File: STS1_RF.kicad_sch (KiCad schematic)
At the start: 74 parts, among them J1 UHF, Q1 SQ2318, U10 TQP3M9036, U11 QPC1022, U2 LP2985-1.8, U4 74LVC2G74, U5 TYKTBCSANF-26.000000, U7 NL17SV04XV5T2G, U8 Si4463, U9 LFCG-490+

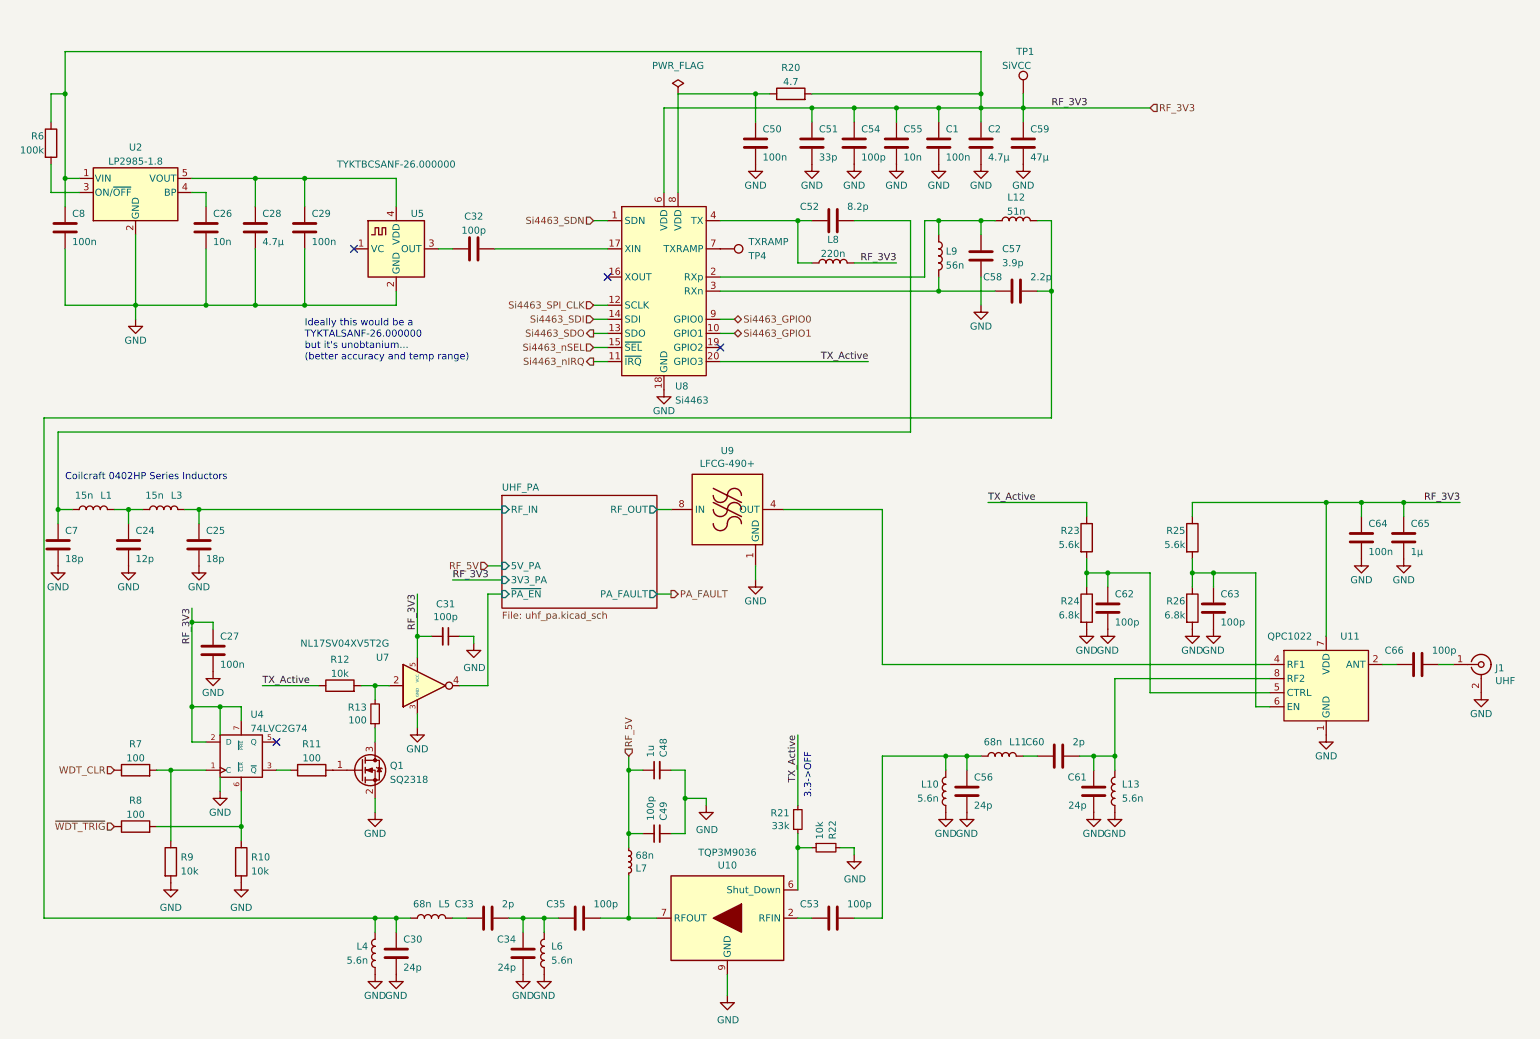
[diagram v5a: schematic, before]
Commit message: feat: clean up schematic
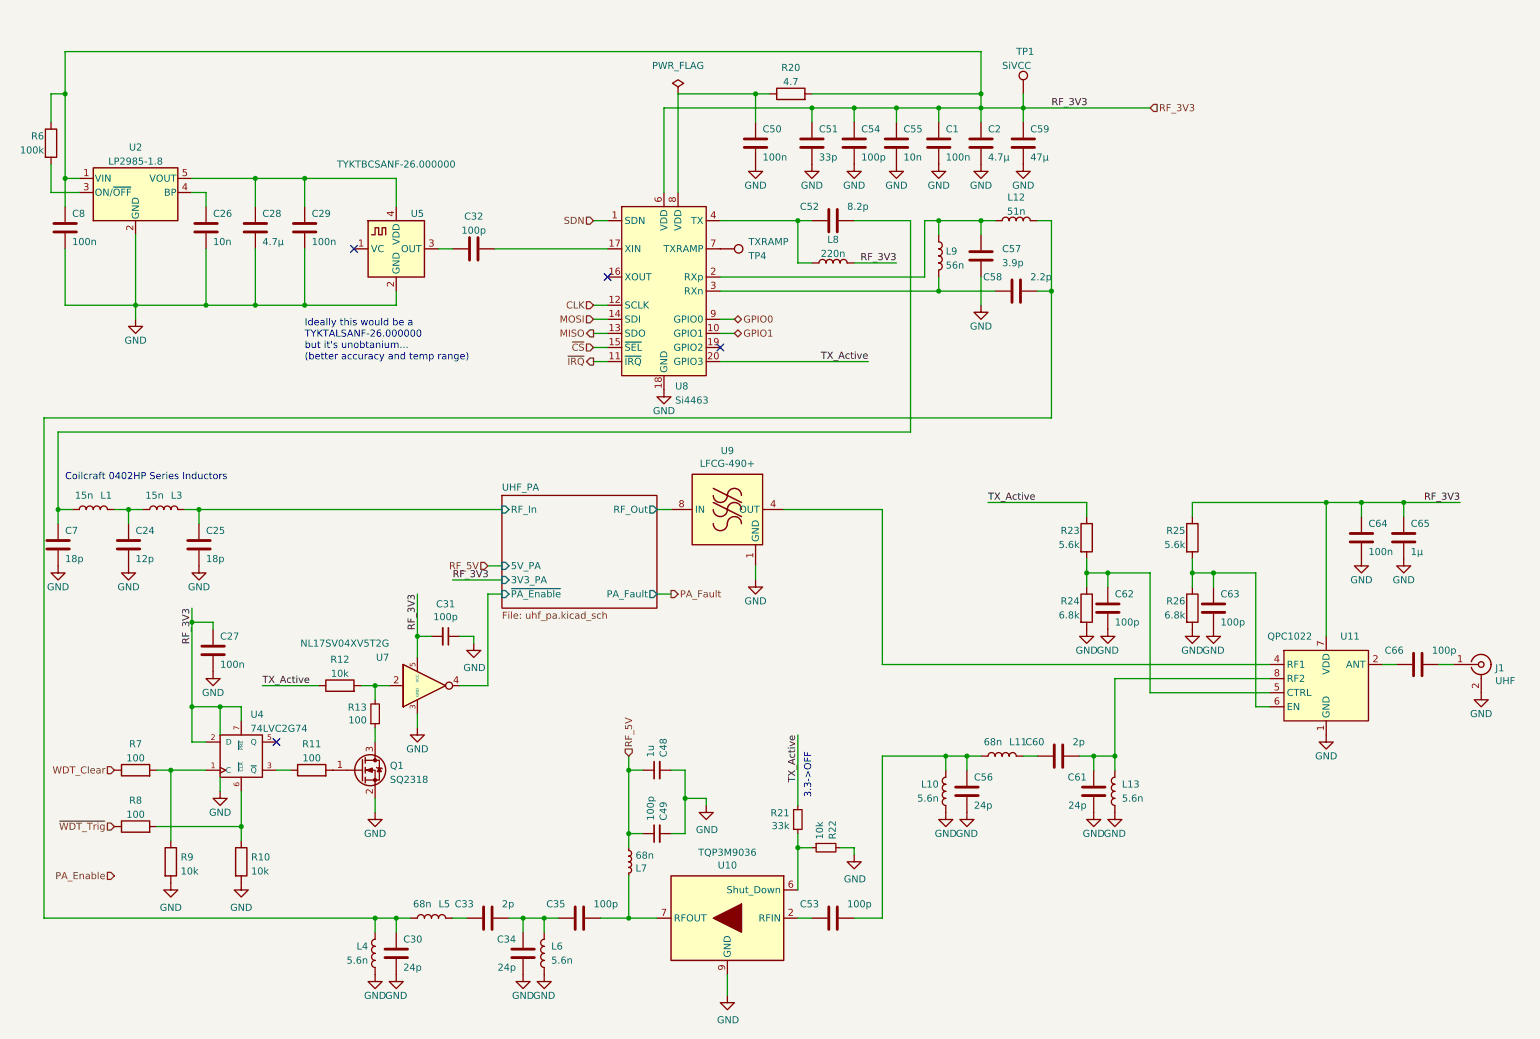
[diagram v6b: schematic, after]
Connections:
- net Si4463_GPIO0 renamed GPIO0
- net Si4463_GPIO1 renamed GPIO1
- net Si4463_SDI renamed MOSI
- net Si4463_SDN renamed SDN
- net Si4463_SDO renamed MISO
- net Si4463_SPI_CLK renamed CLK
- net Si4463_nIRQ renamed ~{IRQ}
- net Si4463_nSEL renamed ~{CS}
- net UHF_PA/RF_IN renamed UHF_PA/RF_In
- net UHF_PA/RF_OUT renamed UHF_PA/RF_Out
- net UHF_PA/~{PA_EN} renamed UHF_PA/~{PA_Enable}
- net WDT_CLR renamed WDT_Clear
- net ~{WDT_TRIG} renamed ~{WDT_Trig}
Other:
- sheet UHF_PA ports: added PA_Fault, RF_In, RF_Out, ~{PA_Enable}; removed PA_FAULT, RF_IN, RF_OUT, ~{PA_EN}

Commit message: feat: update RF hardware and clean up ERC errors
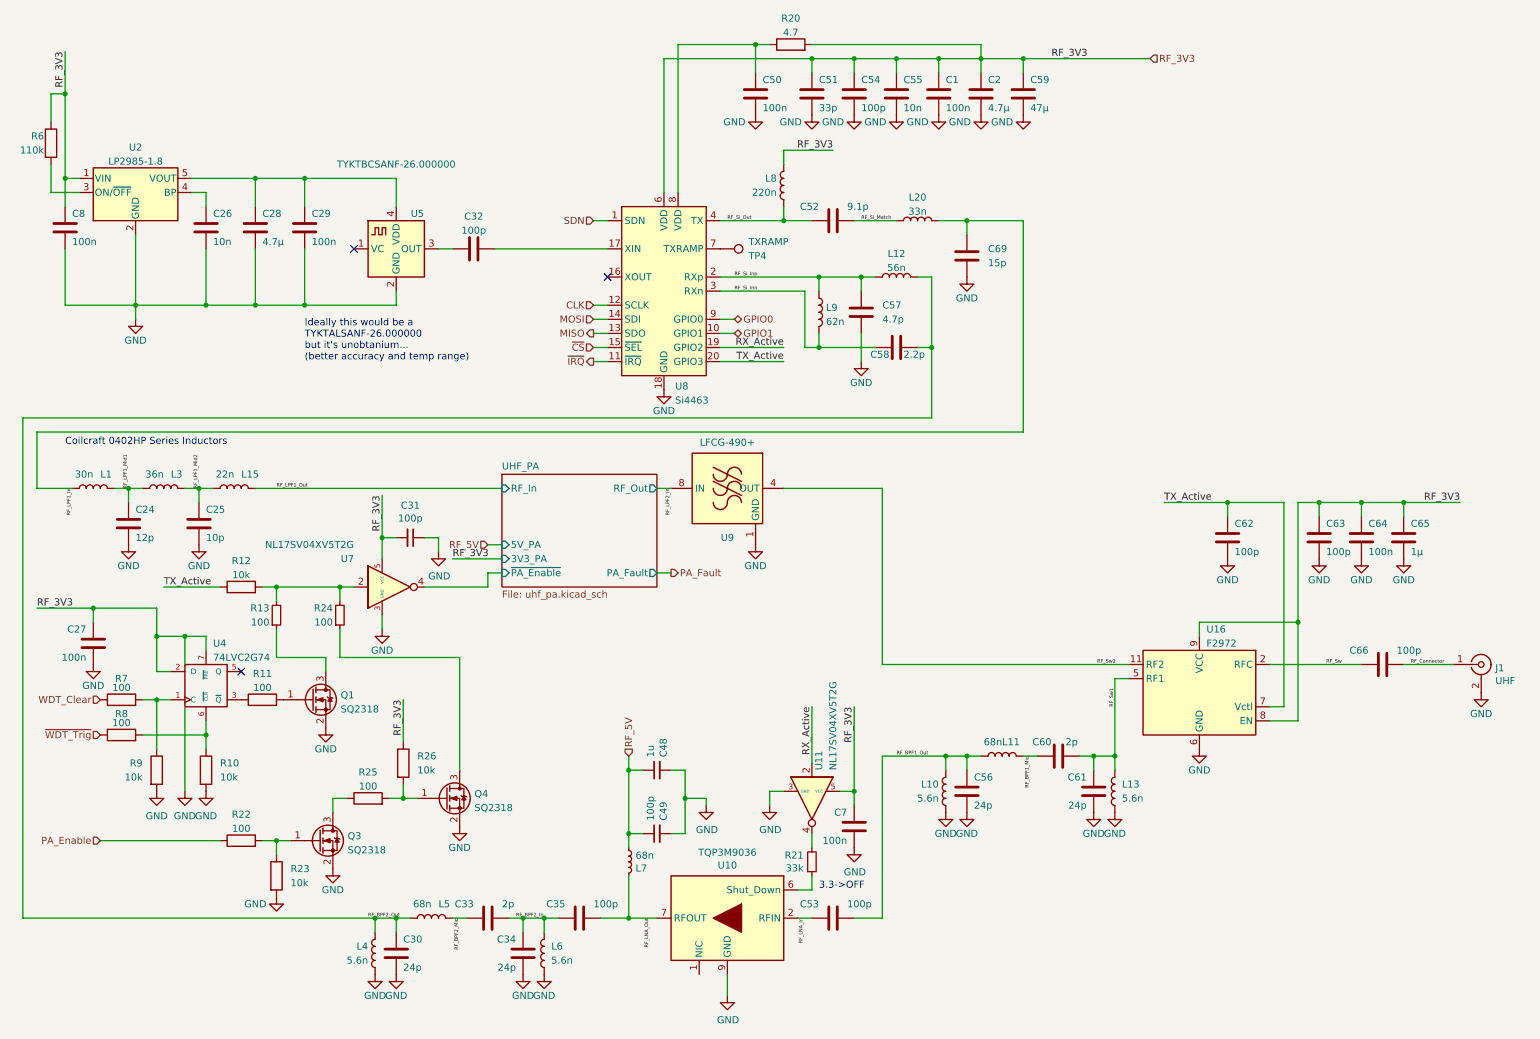
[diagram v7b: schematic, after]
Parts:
- removed R22: 10k, Resistor_SMD:R_0603_1608Metric, symbol Device:R_Small
- removed R24: 6.8k, Resistor_SMD:R_0603_1608Metric, symbol Device:R
- removed TP1: SiVCC, STS1library:STS1_Testpoint, symbol Connector:TestPoint
- removed U11: QPC1022, STS_Package_LGA:Qorvo_9Pin_1.1x1.5mm_LGA, symbol STS_RF_Module:QPC1022
- added C69: 15p, Capacitor_SMD:C_0402_1005Metric, symbol Device:C
- added L15: 22n, Inductor_SMD:L_0402_1005Metric, symbol Device:L
- added L20: 33n, Inductor_SMD:L_0402_1005Metric, symbol Device:L
- added Q3, Q4: SQ2318, Package_TO_SOT_SMD:SOT-23, symbol Device:Q_NMOS_GSD
- added R22: 100, Resistor_SMD:R_0603_1608Metric, symbol Device:R
- added R24: 100, Resistor_SMD:R_0603_1608Metric, symbol Device:R_Small
- added U11: NL17SV04XV5T2G, Package_TO_SOT_SMD:SOT-553, symbol 74xGxx:74LVC1GU04DRL
- added U16: F2972, Package_DFN_QFN:IDT_NEG12_1EP_2x2mm_P0.5mm_EP1.1x1.1mm_ThermalVias, symbol lsf-kicad-lib:F2972
- C25: value 18p -> 10p
- C52: value 8.2p -> 9.1p
- C57: value 3.9p -> 4.7p
- C7: value 18p -> 100n; footprint Capacitor_SMD:C_0402_1005Metric -> Capacitor_SMD:C_0805_2012Metric
- L1: value 15n -> 30n
- L12: value 51n -> 56n
- L3: value 15n -> 36n
- L9: value 56n -> 62n
- R23: value 5.6k -> 10k
- R25: value 5.6k -> 100
- R26: value 6.8k -> 10k
- R6: value 100k -> 110k
- U10: symbol lsf-kicad:TQP3M9036 -> lsf-kicad-lib:TQP3M9036
- U9: symbol lsf-kicad:LFCG-490+ -> lsf-kicad-lib:LFCG-490+
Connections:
- net GND: now also R23.2, C69.2, Q3.2 (S), Q4.2 (S), U11.3 (GND), U16.1 (GND), U16.10 (GND), U16.12 (GND), U16.13 (GND), U16.3 (GND), U16.4 (GND), U16.6 (GND); no longer R26.2
- net PA_Enable: now also R22.1
- net TX_Active: now also C62.1, U16.7 (Vctl); no longer R21.2, R23.1
- net VCC: now also C63.1, C7.1, R26.1, U11.5 (VCC), U16.8 (EN), U16.9 (VCC); no longer R25.1
- net RF_Connector: now reaches C66.2, J1.1 (In)
- net at R12.2, R13.2, U7.2: now also R24.2
- net RF_Sw2: now reaches U9.4 (OUT)
- net RF_Sw2: now also U16.11 (RF2)
- net RF_BPF2_Out: now reaches C30.1, C58.2, L12.2, L4.2, L5.1
- net RF_BPF2_In: now reaches C33.2, C34.1, C35.1, L6.2
- net RF_LNA_Out: now reaches C35.2, L7.1, U10.7 (RFOUT)
- net RF_LPF1_Mid1: now reaches C24.1, L1.2, L3.1
- net RF_BPF2_Mid: now reaches C33.1, L5.2
- net RF_BPF1_Mid: now reaches C60.1, L11.2
- net RF_Sw1: now reaches C60.2, C61.1, L13.2
- net RF_Sw1: now also U16.5 (RF1)
- net RF_Si_Out: now reaches C52.1, L8.1, U8.4 (TX)
- net RF_BPF1_Out: now reaches C53.2, C56.1, L10.2, L11.1
- net RF_LNA_In: now reaches C53.1, U10.2 (RFIN)
- net at U10.1 (NIC): now also U10.3 (NIC), U10.4 (NIC), U10.5 (NIC), U10.8 (NIC)
- net RF_Si_Inp: now reaches C57.1, L12.1, L9.1, U8.2 (RXp)
- net RF_Si_Inn: now reaches C58.1, L9.2, U8.3 (RXn)
- net RF_Sw: now reaches C66.1
- net RF_Sw: now also U16.2 (RFC)
- net RX_Active: now reaches U8.19 (GPIO2)
- net RX_Active: now also U11.2
- net UHF_PA/RF_In renamed RF_LPF1_Mid2
- net RF_LPF1_Mid2: now also L15.1
- net UHF_PA/RF_Out renamed RF_LPF2_In
- new net: R21.2, U11.4
- new net: Q3.1 (G), R22.2, R23.1
- new net: Q3.3 (D), R25.1
- new net: Q4.1 (G), R25.2, R26.2
- new net: Q4.3 (D), R24.1
- new net RF_LPF1_In: C69.1, L1.1, L20.2
- new net RF_LPF1_Out: L15.2
- new net RF_Si_Match: C52.2, L20.1
- no-connect marks 4 -> 3
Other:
- moved on the sheet: C1, C2, C24, C25, C27, C31, C50, C51, C54, C55, C57, C58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

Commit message: feat: more schematic cleanup
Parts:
- U16: footprint Package_DFN_QFN:IDT_NEG12_1EP_2x2mm_P0.5mm_EP1.1x1.1mm_ThermalVias -> lsf-kicad-lib:IDT_NEG-12-1EP_2x2mm_P0.5mm_EP1.1x1.1mm_ThermalVias
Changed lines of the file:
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@@
       (effects (font (size 1.27 1.27)) (justify right))
     )
-    (property "Footprint" "Package_DFN_QFN:IDT_NEG12_1EP_2x2mm_P0.5mm_EP1.1x1.1mm_ThermalVias" (id 2) (at 246.38 123.19 0)
+    (property "Footprint" "lsf-kicad-lib:IDT_NEG-12-1EP_2x2mm_P0.5mm_EP1.1x1.1mm_ThermalVias" (id 2) (at 246.38 123.19 0)
       (effects (font (size 1.27 1.27)) hide)
     )
